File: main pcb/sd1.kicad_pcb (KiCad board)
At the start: 2 copper layers, 66.1 x 60 mm, 14 parts

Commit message: fixed con2
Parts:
- ARCADE_PCB_CONN1: footprint Connector_Harwin:Harwin_Gecko-G125-FVX1205L0X_2x06_P1.25mm_Vertical -> Connector_PinHeader_2.54mm:PinHeader_2x06_P2.54mm_Vertical
- moved ARCADE_PCB_CONN1 4.30 mm to (174.0, 111.3), turned to 180 degrees
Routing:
- net ARC7: track 43.4 -> 14.7 mm
- net ARC8: track 38.1 -> 11.0 mm
- net ARC9: track 32.9 -> 7.76 mm
- net ARC10: track 24.3 -> 3.85 mm
- net ARC5: track 22.0 -> 12.2 mm
- net ARC6: track 19.7 -> 11.4 mm
- net 3.3V: track 219.5 -> 211.6 mm
- net ARC1: track 31.2 -> 23.5 mm
- net ARC2: track 28.9 -> 22.2 mm
- net ARC3: track 26.6 -> 21.3 mm
- net ARC4: track 24.3 -> 20.8 mm

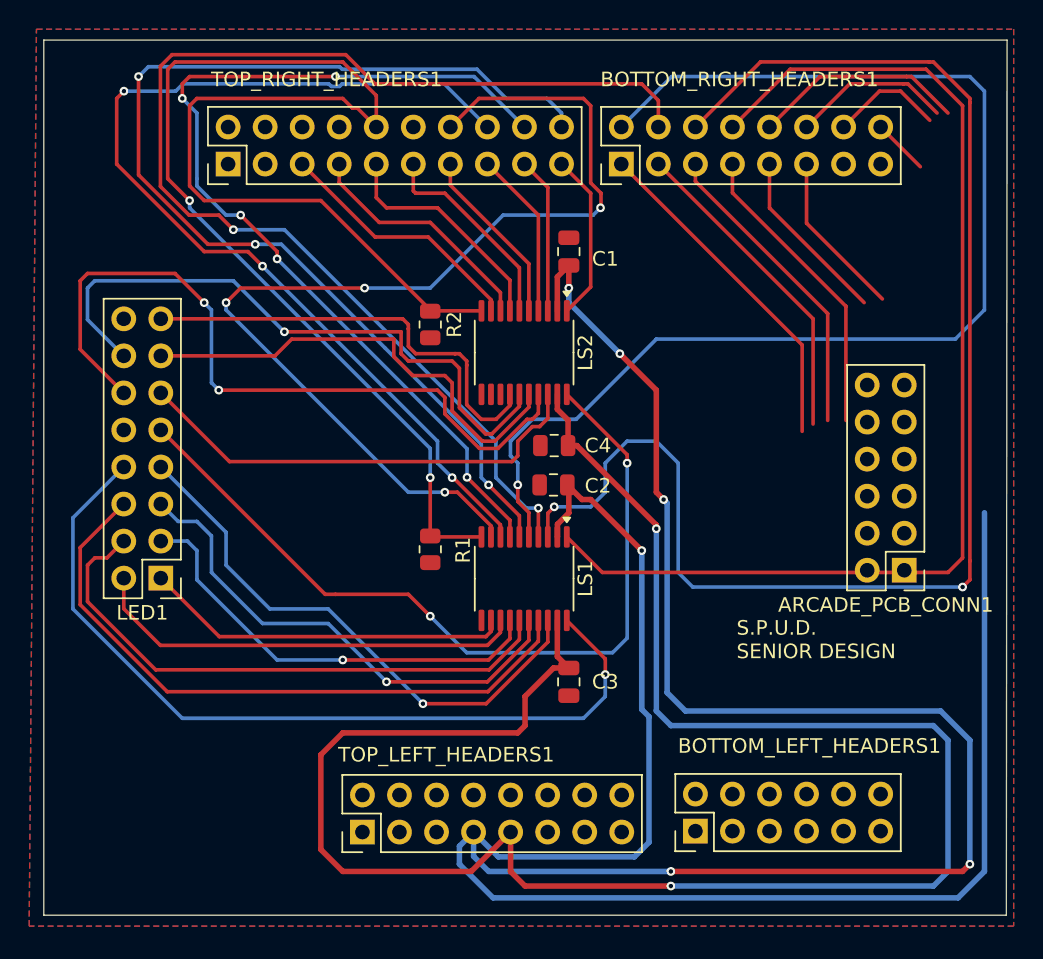
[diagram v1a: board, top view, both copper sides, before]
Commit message: wired new connector
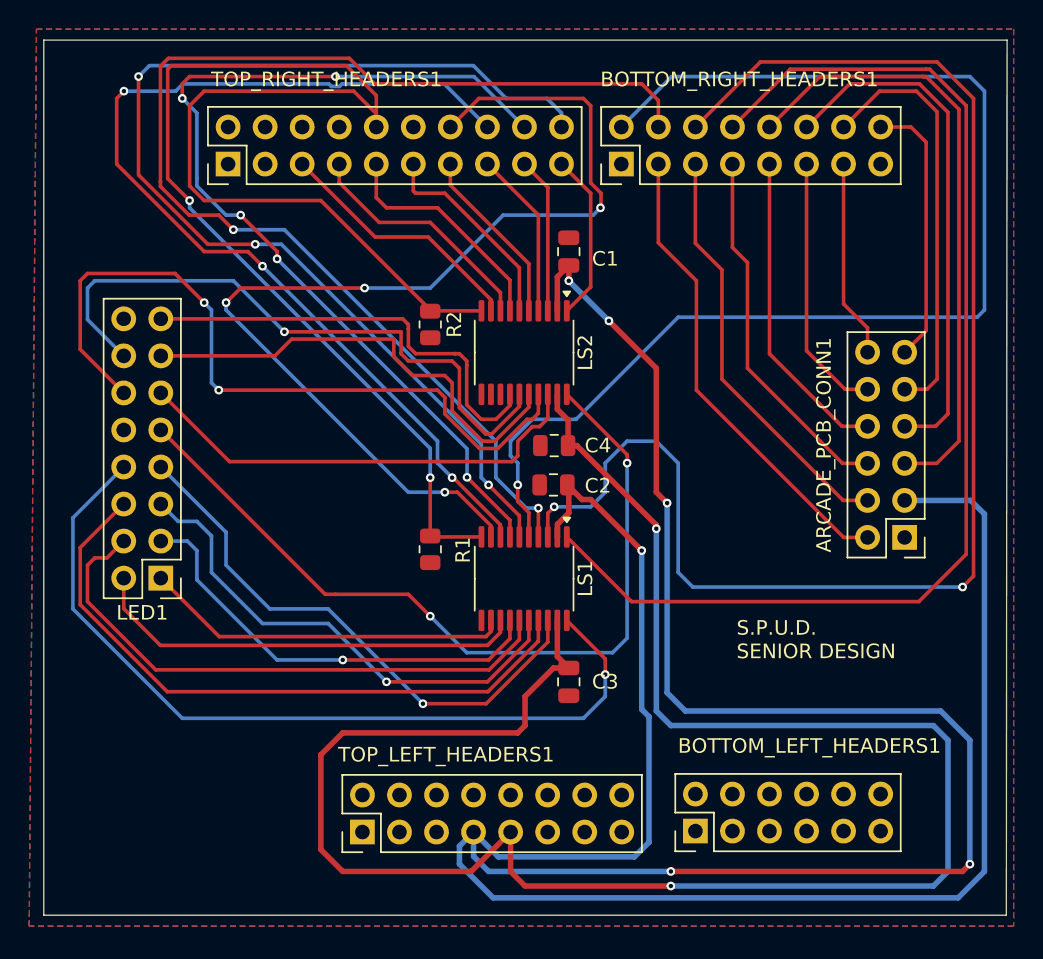
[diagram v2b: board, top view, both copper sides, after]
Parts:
- moved ARCADE_PCB_CONN1 2.25 mm to (174.0, 109.1)
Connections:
- ARCADE_PCB_CONN1 pad 1: ARC1 -> GND
- ARCADE_PCB_CONN1 pad 10: ARC10 -> ARC5
- ARCADE_PCB_CONN1 pad 11: 3.3V -> ARC10
- ARCADE_PCB_CONN1 pad 12: GND -> ARC6
- ARCADE_PCB_CONN1 pad 2: ARC2 -> ARC1
- ARCADE_PCB_CONN1 pad 3: ARC3 -> 3.3V
- ARCADE_PCB_CONN1 pad 4: ARC4 -> ARC2
- ARCADE_PCB_CONN1 pad 5: ARC5 -> ARC7
- ARCADE_PCB_CONN1 pad 6: ARC6 -> ARC3
- ARCADE_PCB_CONN1 pad 7: ARC7 -> ARC8
- ARCADE_PCB_CONN1 pad 8: ARC8 -> ARC4
- BOTTOM_RIGHT_HEADERS1 pad 1: ARC1 -> unconnected-(BOTTOM_RIGHT_HEADERS1-IO-Pad1)
- BOTTOM_RIGHT_HEADERS1 pad 11: ARC6 -> ARC5
- BOTTOM_RIGHT_HEADERS1 pad 13: unconnected-(BOTTOM_RIGHT_HEADERS1-IO-Pad13) -> ARC6
- BOTTOM_RIGHT_HEADERS1 pad 3: ARC2 -> ARC1
- BOTTOM_RIGHT_HEADERS1 pad 5: ARC3 -> ARC2
- BOTTOM_RIGHT_HEADERS1 pad 7: ARC4 -> ARC3
- BOTTOM_RIGHT_HEADERS1 pad 9: ARC5 -> ARC4
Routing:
- net ARC7: track 14.7 -> 42.5 mm
- net ARC8: track 11.0 -> 35.7 mm
- net ARC9: track 7.76 -> 28.9 mm
- net ARC10: track 3.85 -> 18.6 mm
- net ARC1: track 23.5 -> 32.5 mm
- net ARC2: track 22.2 -> 28.9 mm
- net ARC5: track 12.2 -> 18.1 mm
- net 3.3V: track 211.6 -> 217.4 mm
- net ARC3: track 21.3 -> 25.4 mm
- net ARC6: track 11.4 -> 13.6 mm
- net DATA1: track 78.0 -> 80.0 mm
- net ARC4: track 20.8 -> 21.8 mm
- net OE: track 104.0 -> 104.7 mm
